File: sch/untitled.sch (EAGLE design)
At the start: 25 parts, among them J1 AVR_SPI_PRG_62X3_LOCK, Q1 20MHz, U1 ATMEGA328P, X1 SM06B-SSR-H-TB

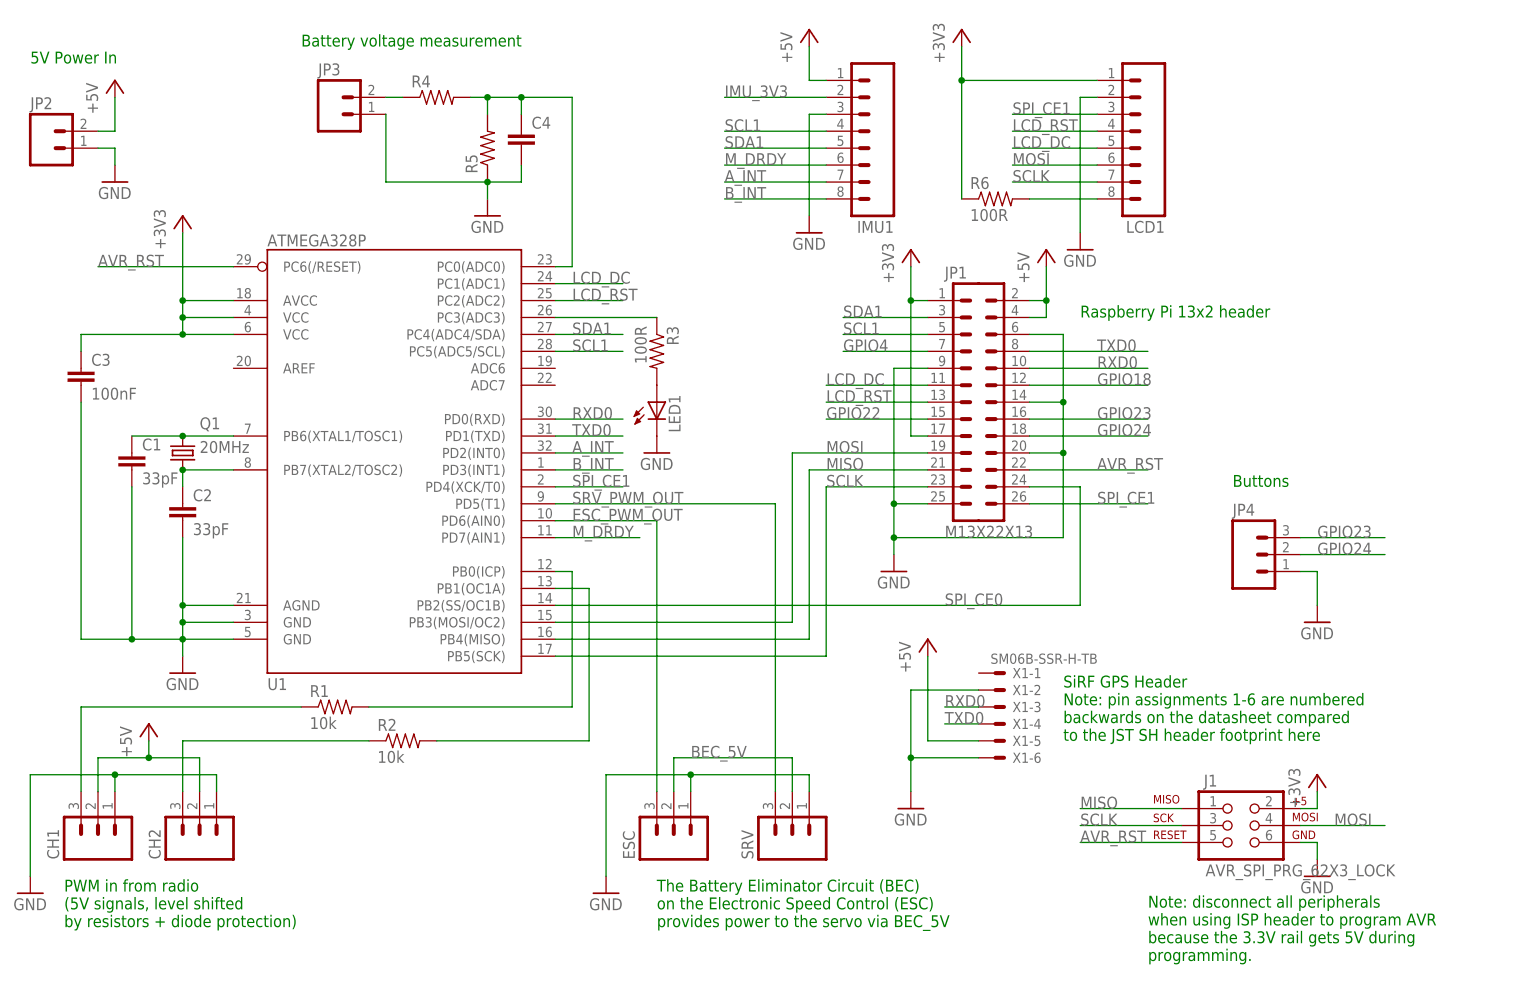
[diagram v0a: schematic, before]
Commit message: critical PCB connector fixes
 - flipped RPi connector around to correct orientation
 - flipped SiRF GPS connector around
 - added two more resistors to radio input, so there's a resistor
   divider instead of relying on overload protection
 - powered LCD backlight LED by 5v instead of 3.3v, resistor can adjust
   brightness
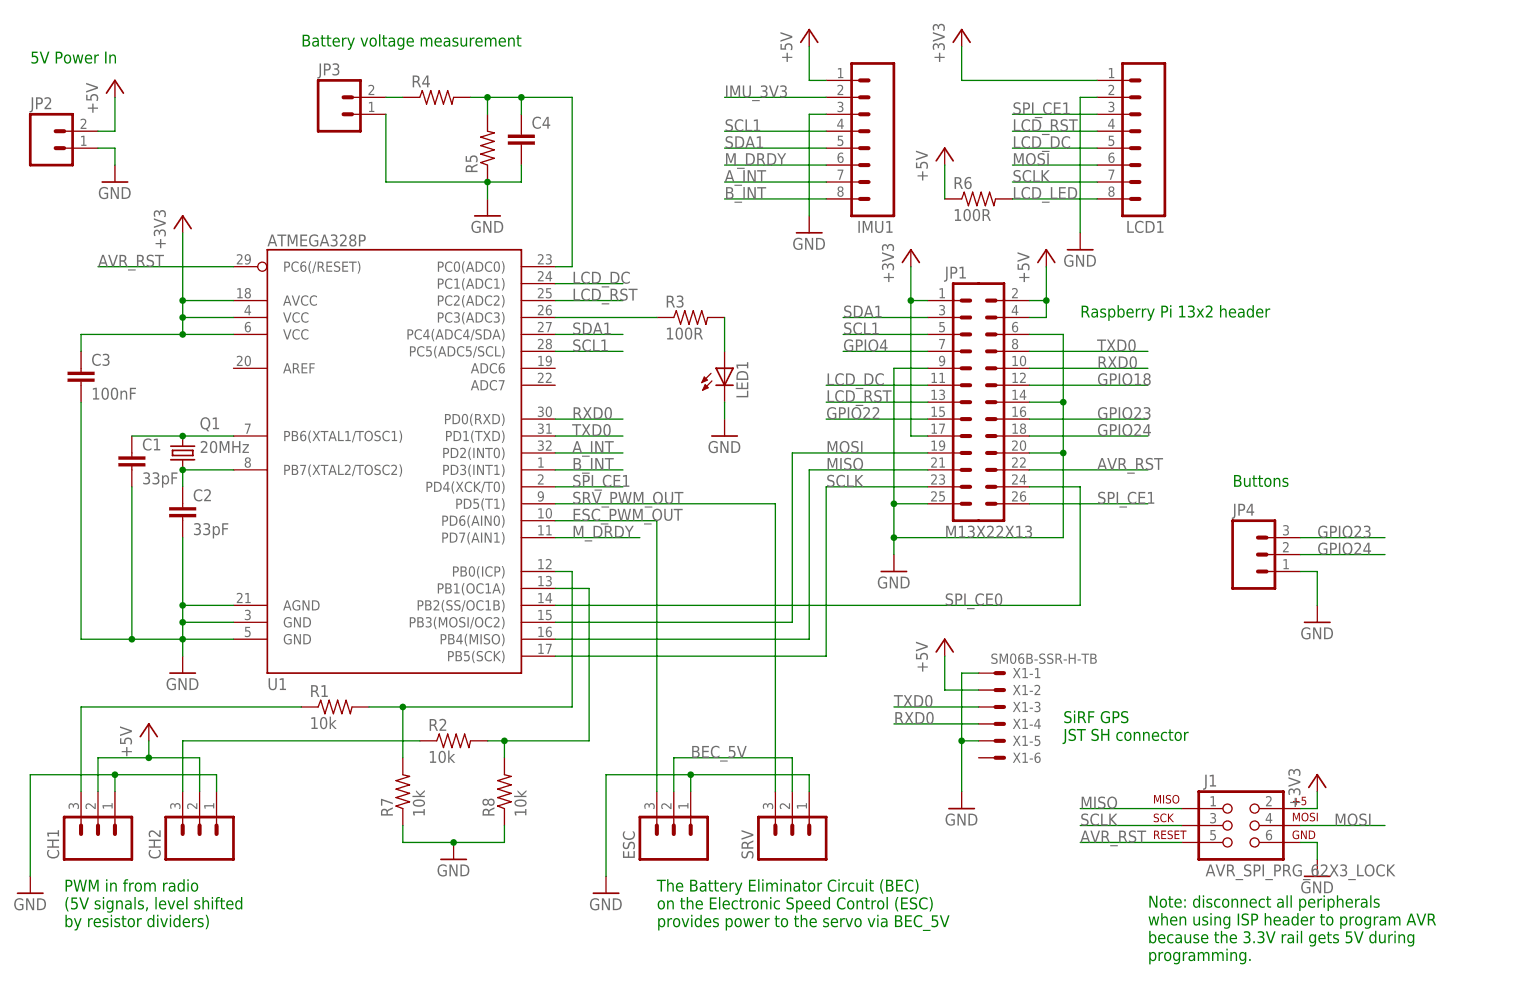
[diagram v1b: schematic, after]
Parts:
- added R7, R8: 10k, SparkFun-Resistors:RESISTOR0805-RES
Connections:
- net N$7 renamed LCD_LED
- net +3V3: no longer R6.1
- net +5V: now also R6.1, X1-2.S; no longer X1-5.S
- net GND: now also R7.1, R8.1, X1-1.S, X1-5.S; no longer X1-2.S, X1-6.S
- net N$4: now also R7.2
- net N$5: now also R8.2
- net RXD0: now also X1-4.S; no longer X1-3.S
- net TXD0: now also X1-3.S; no longer X1-4.S
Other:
- note added: "PWM in from radio (5V signals, level shifted by resistor dividers)"
- note added: "SiRF GPS JST SH connector"
- note removed: "PWM in from radio (5V signals, level shifted by resistors + diode protection)"
- note removed: "SiRF GPS Header Note: pin assignments 1-6 are numbered backwards on the datasheet compared to the JST SH header footprint here"
- moved on the sheet: LED1, R2, R3, R6
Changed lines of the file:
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@@
 <part name="JP4" library="SparkFun-Connectors" deviceset="M03" device="POLAR_LOCK"/>
 <part name="GND12" library="SparkFun-Aesthetics" deviceset="GND" device=""/>
+<part name="R7" library="SparkFun-Resistors" deviceset="RESISTOR" device="0805-RES" value="10k"/>
+<part name="R8" library="SparkFun-Resistors" deviceset="RESISTOR" device="0805-RES" value="10k"/>
+<part name="GND13" library="SparkFun-Aesthetics" deviceset="GND" device=""/>
+<part name="P+6" library="supply1" deviceset="+5V" device=""/>
 </parts>
 <sheets>
@@
 <text x="10.16" y="-12.7" size="1.778" layer="91">PWM in from radio
 (5V signals, level shifted
-by resistors + diode protection)</text>
+by resistor dividers)</text>
 <text x="5.08" y="116.84" size="1.778" layer="91">5V Power In</text>
 <text x="45.72" y="119.38" size="1.778" layer="91">Battery voltage measurement</text>
-<text x="160.02" y="15.24" size="1.778" layer="91">SiRF GPS Header
-Note: pin assignments 1-6 are numbered
-backwards on the datasheet compared
-to the JST SH header footprint here</text>
+<text x="160.02" y="15.24" size="1.778" layer="91">SiRF GPS
+JST SH connector</text>
 <text x="172.72" y="-17.78" size="1.778" layer="91">Note: disconnect all peripherals
 when using ISP header to program AVR
@@
 <instance part="GND3" gate="1" x="5.08" y="-7.62"/>
 <instance part="GND4" gate="1" x="91.44" y="-7.62"/>
-<instance part="GND5" gate="1" x="137.16" y="5.08"/>
-<instance part="P+3" gate="1" x="139.7" y="30.48"/>
+<instance part="GND5" gate="1" x="144.78" y="5.08"/>
+<instance part="P+3" gate="1" x="142.24" y="30.48"/>
 <instance part="P+4" gate="1" x="121.92" y="121.92"/>
 <instance part="GND6" gate="1" x="121.92" y="91.44"/>
@@
 <instance part="P+5" gate="1" x="17.78" y="114.3"/>
 <instance part="GND7" gate="1" x="17.78" y="99.06"/>
-<instance part="LED1" gate="G$1" x="99.06" y="66.04"/>
-<instance part="GND8" gate="1" x="99.06" y="58.42"/>
-<instance part="R3" gate="G$1" x="99.06" y="73.66" rot="R270"/>
+<instance part="LED1" gate="G$1" x="109.22" y="71.12"/>
+<instance part="GND8" gate="1" x="109.22" y="60.96"/>
+<instance part="R3" gate="G$1" x="104.14" y="78.74"/>
 <instance part="R1" gate="G$1" x="50.8" y="20.32"/>
-<instance part="R2" gate="G$1" x="60.96" y="15.24"/>
+<instance part="R2" gate="G$1" x="68.58" y="15.24"/>
 <instance part="JP3" gate="G$1" x="50.8" y="109.22"/>
 <instance part="GND9" gate="1" x="73.66" y="93.98"/>
@@
 <instance part="+3V3" gate="G$1" x="144.78" y="121.92"/>
 <instance part="GND10" gate="1" x="162.56" y="88.9"/>
-<instance part="R6" gate="G$1" x="149.86" y="96.52"/>
+<instance part="R6" gate="G$1" x="147.32" y="96.52"/>
 <instance part="J1" gate="G$1" x="185.42" y="2.54"/>
 <instance part="+3V4" gate="G$1" x="198.12" y="10.16"/>
@@
 <instance part="JP4" gate="G$1" x="187.96" y="43.18"/>
 <instance part="GND12" gate="1" x="198.12" y="33.02"/>
+<instance part="R7" gate="G$1" x="60.96" y="7.62" rot="R90"/>
+<instance part="R8" gate="G$1" x="76.2" y="7.62" rot="R90"/>
+<instance part="GND13" gate="1" x="68.58" y="-2.54"/>
+<instance part="P+6" gate="1" x="142.24" y="104.14"/>
 </instances>
 <busses>
@@
 </segment>
 <segment>
-<pinref part="X1" gate="-6" pin="S"/>
-<pinref part="GND5" gate="1" pin="GND"/>
-<wire x1="147.32" y1="12.7" x2="137.16" y2="12.7" width="0.1524" layer="91"/>
-<wire x1="137.16" y1="12.7" x2="137.16" y2="7.62" width="0.1524" layer="91"/>
-<pinref part="X1" gate="-2" pin="S"/>
-<wire x1="147.32" y1="22.86" x2="137.16" y2="22.86" width="0.1524" layer="91"/>
-<wire x1="137.16" y1="22.86" x2="137.16" y2="12.7" width="0.1524" layer="91"/>
-<junction x="137.16" y="12.7"/>
-</segment>
-<segment>
 <pinref part="IMU1" gate="G$1" pin="3"/>
 <pinref part="GND6" gate="1" pin="GND"/>
@@
 <pinref part="LED1" gate="G$1" pin="C"/>
 <pinref part="GND8" gate="1" pin="GND"/>
+<wire x1="109.22" y1="63.5" x2="109.22" y2="66.04" width="0.1524" layer="91"/>
 </segment>
 <segment>
@@
 <wire x1="195.58" y1="40.64" x2="198.12" y2="40.64" width="0.1524" layer="91"/>
 <wire x1="198.12" y1="40.64" x2="198.12" y2="35.56" width="0.1524" layer="91"/>
+</segment>
+<segment>
+<pinref part="X1" gate="-1" pin="S"/>
+<pinref part="GND5" gate="1" pin="GND"/>
+<wire x1="147.32" y1="25.4" x2="144.78" y2="25.4" width="0.1524" layer="91"/>
+<wire x1="144.78" y1="25.4" x2="144.78" y2="15.24" width="0.1524" layer="91"/>
+<pinref part="X1" gate="-5" pin="S"/>
+<wire x1="144.78" y1="15.24" x2="144.78" y2="7.62" width="0.1524" layer="91"/>
+<wire x1="147.32" y1="15.24" x2="144.78" y2="15.24" width="0.1524" layer="91"/>
+<junction x="144.78" y="15.24"/>
+</segment>
+<segment>
+<pinref part="GND13" gate="1" pin="GND"/>
+<pinref part="R7" gate="G$1" pin="1"/>
+<wire x1="68.58" y1="0" x2="60.96" y2="0" width="0.1524" layer="91"/>
+<wire x1="60.96" y1="0" x2="60.96" y2="2.54" width="0.1524" layer="91"/>
+<pinref part="R8" gate="G$1" pin="1"/>
+<wire x1="68.58" y1="0" x2="76.2" y2="0" width="0.1524" layer="91"/>
+<wire x1="76.2" y1="0" x2="76.2" y2="2.54" width="0.1524" layer="91"/>
+<junction x="68.58" y="0"/>
 </segment>
 </net>
@@
 <wire x1="165.1" y1="114.3" x2="144.78" y2="114.3" width="0.1524" layer="91"/>
 <wire x1="144.78" y1="114.3" x2="144.78" y2="119.38" width="0.1524" layer="91"/>
-<pinref part="R6" gate="G$1" pin="1"/>
-<wire x1="144.78" y1="96.52" x2="144.78" y2="114.3" width="0.1524" layer="91"/>
-<junction x="144.78" y="114.3"/>
 </segment>
 <segment>
@@
 <wire x1="157.48" y1="78.74" x2="157.48" y2="81.28" width="0.1524" layer="91"/>
 <junction x="157.48" y="81.28"/>
-</segment>
-<segment>
-<pinref part="P+3" gate="1" pin="+5V"/>
-<pinref part="X1" gate="-5" pin="S"/>
-<wire x1="139.7" y1="27.94" x2="139.7" y2="15.24" width="0.1524" layer="91"/>
-<wire x1="139.7" y1="15.24" x2="147.32" y2="15.24" width="0.1524" layer="91"/>
 </segment>
 <segment>
@@
 <wire x1="17.78" y1="106.68" x2="17.78" y2="111.76" width="0.1524" layer="91"/>
 </segment>
+<segment>
+<pinref part="X1" gate="-2" pin="S"/>
+<pinref part="P+3" gate="1" pin="+5V"/>
+<wire x1="147.32" y1="22.86" x2="142.24" y2="22.86" width="0.1524" layer="91"/>
+<wire x1="142.24" y1="22.86" x2="142.24" y2="27.94" width="0.1524" layer="91"/>
+</segment>
+<segment>
+<pinref part="P+6" gate="1" pin="+5V"/>
+<pinref part="R6" gate="G$1" pin="1"/>
+<wire x1="142.24" y1="101.6" x2="142.24" y2="96.52" width="0.1524" layer="91"/>
+</segment>
 </net>
 <net name="SDA1" class="0">
@@
 <wire x1="86.36" y1="40.64" x2="83.82" y2="40.64" width="0.1524" layer="91"/>
 <pinref part="R1" gate="G$1" pin="2"/>
-<wire x1="55.88" y1="20.32" x2="86.36" y2="20.32" width="0.1524" layer="91"/>
+<wire x1="55.88" y1="20.32" x2="60.96" y2="20.32" width="0.1524" layer="91"/>
+<pinref part="R7" gate="G$1" pin="2"/>
+<wire x1="60.96" y1="20.32" x2="86.36" y2="20.32" width="0.1524" layer="91"/>
+<wire x1="60.96" y1="12.7" x2="60.96" y2="20.32" width="0.1524" layer="91"/>
+<junction x="60.96" y="20.32"/>
 </segment>
 </net>
@@
 <wire x1="88.9" y1="38.1" x2="83.82" y2="38.1" width="0.1524" layer="91"/>
 <pinref part="R2" gate="G$1" pin="2"/>
-<wire x1="66.04" y1="15.24" x2="88.9" y2="15.24" width="0.1524" layer="91"/>
+<wire x1="73.66" y1="15.24" x2="76.2" y2="15.24" width="0.1524" layer="91"/>
+<pinref part="R8" gate="G$1" pin="2"/>
+<wire x1="76.2" y1="15.24" x2="88.9" y2="15.24" width="0.1524" layer="91"/>
+<wire x1="76.2" y1="12.7" x2="76.2" y2="15.24" width="0.1524" layer="91"/>
+<junction x="76.2" y="15.24"/>
 </segment>
 </net>
@@
 </segment>
 <segment>
-<pinref part="X1" gate="-4" pin="S"/>
-<wire x1="147.32" y1="17.78" x2="142.24" y2="17.78" width="0.1524" layer="91"/>
-<label x="142.24" y="17.78" size="1.778" layer="95"/>
-</segment>
-<segment>
 <pinref part="U1" gate="G$1" pin="PD1(TXD)"/>
 <wire x1="83.82" y1="60.96" x2="93.98" y2="60.96" width="0.1524" layer="91"/>
 <label x="86.36" y="60.96" size="1.778" layer="95"/>
 </segment>
+<segment>
+<pinref part="X1" gate="-3" pin="S"/>
+<wire x1="147.32" y1="20.32" x2="134.62" y2="20.32" width="0.1524" layer="91"/>
+<label x="134.62" y="20.32" size="1.778" layer="95"/>
+</segment>
 </net>
 <net name="RXD0" class="0">
@@
 </segment>
 <segment>
-<pinref part="X1" gate="-3" pin="S"/>
-<wire x1="147.32" y1="20.32" x2="142.24" y2="20.32" width="0.1524" layer="91"/>
-<label x="142.24" y="20.32" size="1.778" layer="95"/>
-</segment>
-<segment>
 <pinref part="U1" gate="G$1" pin="PD0(RXD)"/>
 <wire x1="83.82" y1="63.5" x2="93.98" y2="63.5" width="0.1524" layer="91"/>
 <label x="86.36" y="63.5" size="1.778" layer="95"/>
+</segment>
+<segment>
+<pinref part="X1" gate="-4" pin="S"/>
+<wire x1="147.32" y1="17.78" x2="134.62" y2="17.78" width="0.1524" layer="91"/>
+<label x="134.62" y="17.78" size="1.778" layer="95"/>
 </segment>
 </net>
@@
 <pinref part="R3" gate="G$1" pin="2"/>
 <pinref part="LED1" gate="G$1" pin="A"/>
+<wire x1="109.22" y1="78.74" x2="109.22" y2="73.66" width="0.1524" layer="91"/>
 </segment>
 </net>
@@
 <wire x1="27.94" y1="7.62" x2="27.94" y2="15.24" width="0.1524" layer="91"/>
 <pinref part="R2" gate="G$1" pin="1"/>
-<wire x1="27.94" y1="15.24" x2="55.88" y2="15.24" width="0.1524" layer="91"/>
+<wire x1="27.94" y1="15.24" x2="63.5" y2="15.24" width="0.1524" layer="91"/>
 </segment>
 </net>
@@
 </segment>
 </net>
-<net name="N$7" class="0">
+<net name="LCD_LED" class="0">
 <segment>
 <pinref part="LCD1" gate="G$1" pin="8"/>
 <pinref part="R6" gate="G$1" pin="2"/>
-<wire x1="165.1" y1="96.52" x2="154.94" y2="96.52" width="0.1524" layer="91"/>
-</segment>
-</net>
+<wire x1="165.1" y1="96.52" x2="152.4" y2="96.52" width="0.1524" layer="91"/>
+<label x="152.4" y="96.52" size="1.778" layer="95"/>
+</segment>
+</net>
